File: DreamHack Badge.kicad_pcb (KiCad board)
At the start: 2 copper layers, 185.4 x 124.5 mm, 0 parts

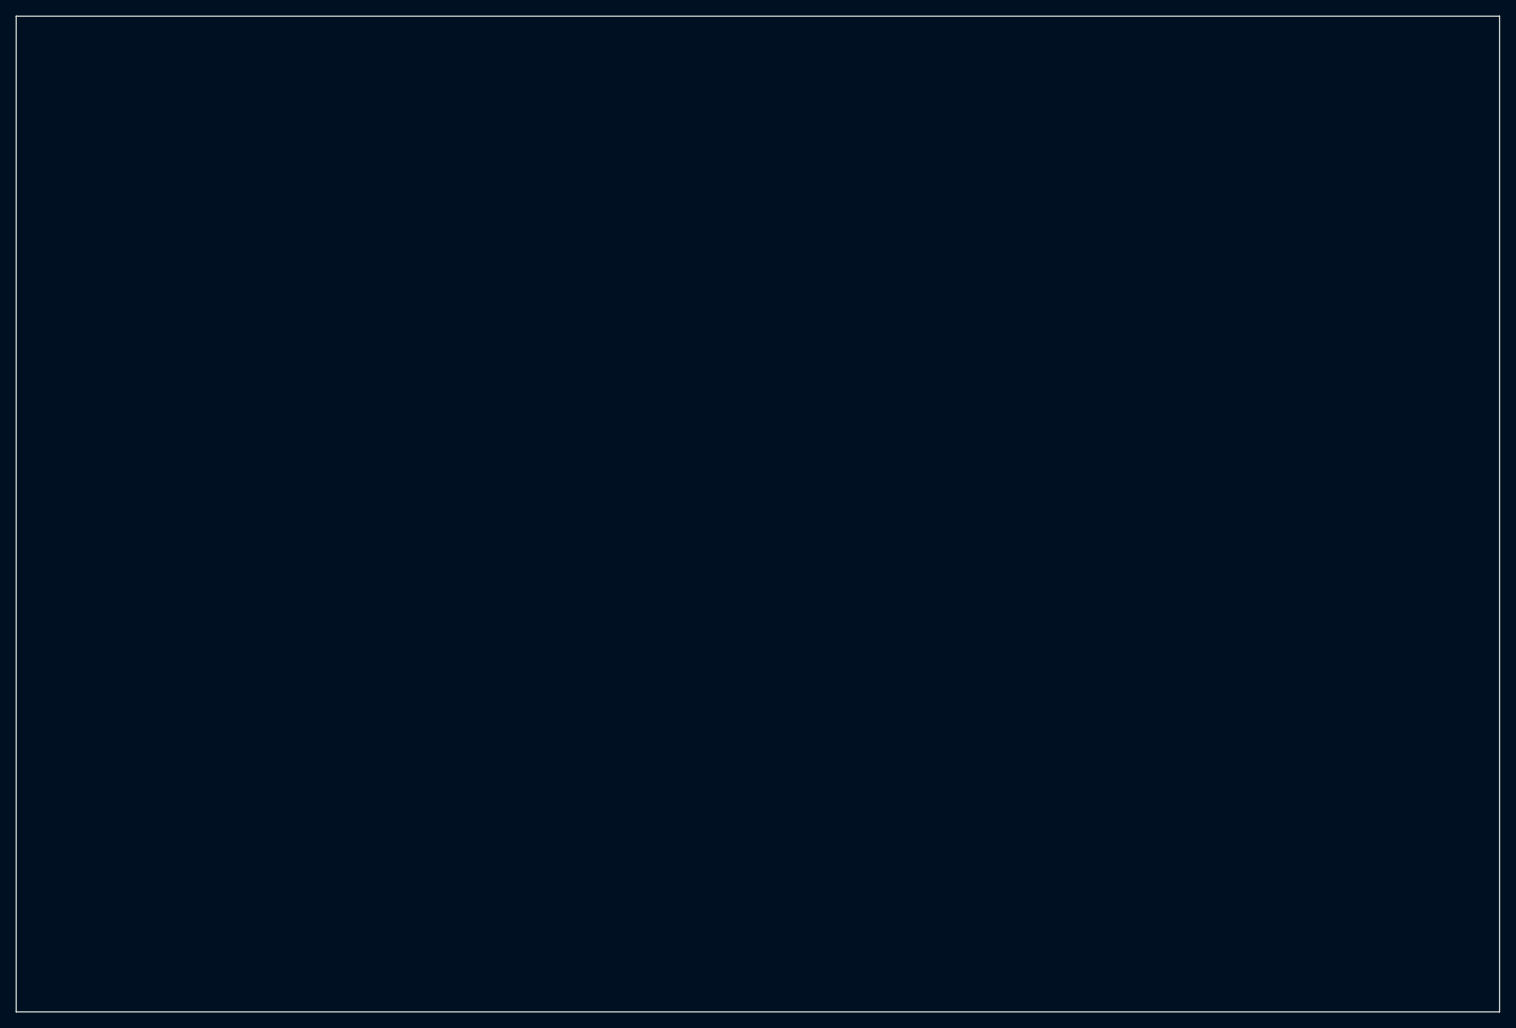
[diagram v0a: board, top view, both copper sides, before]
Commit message: fixed apa102 refs
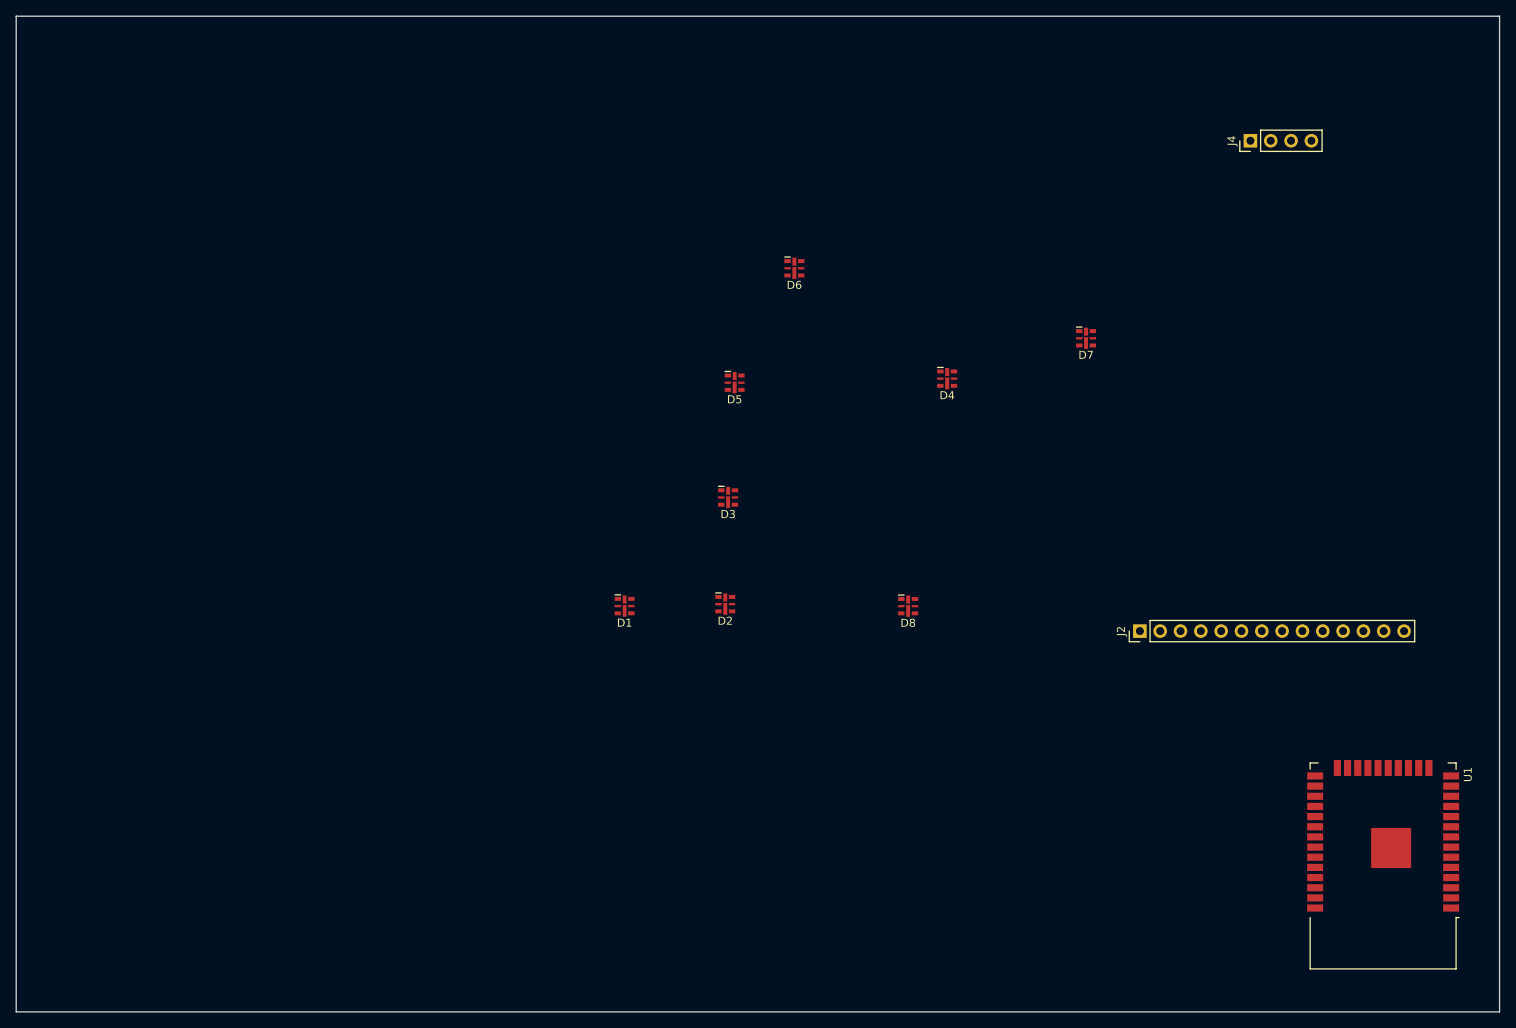
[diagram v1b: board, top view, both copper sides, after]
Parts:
- added D1: APA102-2020, LED_SMD:LED-APA102-2020, F.Cu at (121.8, 99.1)
- added D2: APA102-2020, LED_SMD:LED-APA102-2020, F.Cu at (134.4, 98.9)
- added D3: APA102-2020, LED_SMD:LED-APA102-2020, F.Cu at (134.7, 85.6)
- added D4: APA102-2020, LED_SMD:LED-APA102-2020, F.Cu at (162.1, 70.7)
- added D5: APA102-2020, LED_SMD:LED-APA102-2020, F.Cu at (135.5, 71.2)
- added D6: APA102-2020, LED_SMD:LED-APA102-2020, F.Cu at (143.0, 56.9)
- added D7: APA102-2020, LED_SMD:LED-APA102-2020, F.Cu at (179.5, 65.7)
- added D8: APA102-2020, LED_SMD:LED-APA102-2020, F.Cu at (157.2, 99.2)
- added J2: Conn_01x14_Female, Pin_Headers:Pin_Header_Straight_1x14_Pitch2.54mm, F.Cu at (186.2, 102.3)
- added J4: Conn_01x04_Female, Pin_Headers:Pin_Header_Straight_1x04_Pitch2.54mm, F.Cu at (200.0, 41.0)
- added U1: ESP32-WROOM-32, RF_Modules_Local:ESP32-WROOM-32, F.Cu at (216.6, 128.6)

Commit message: basic pcb layout
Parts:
- moved D4 122.1 mm to (62.1, 140.8)
- moved D5 82.0 mm to (61.5, 35.9)
- moved D1 74.5 mm to (183.4, 140.9)
- moved D3 63.1 mm to (104.5, 141.0)
- moved D8 63.0 mm to (168.1, 37.1)
- moved D7 51.4 mm to (136.9, 36.9)
- moved D2 43.1 mm to (143.8, 140.9)
- moved D6 41.3 mm to (106.9, 36.8)
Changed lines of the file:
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@@
   )
   (module LED_SMD:LED-APA102-2020 (layer F.Cu)
-    (at 157.2124 99.1506)
+    (at 168.148 37.1094)
     (descr http://www.led-color.com/upload/201604/APA102-2020%20SMD%20LED.pdf)
     (tags "LED RGB SPI")
@@
   )
   (module LED_SMD:LED-APA102-2020 (layer F.Cu)
-    (at 162.091 70.7026)
+    (at 62.0776 140.8176)
     (descr http://www.led-color.com/upload/201604/APA102-2020%20SMD%20LED.pdf)
     (tags "LED RGB SPI")
@@
   )
   (module LED_SMD:LED-APA102-2020 (layer F.Cu)
-    (at 179.451 65.659)
+    (at 136.8688 36.946)
     (descr http://www.led-color.com/upload/201604/APA102-2020%20SMD%20LED.pdf)
     (tags "LED RGB SPI")
@@
   )
   (module LED_SMD:LED-APA102-2020 (layer F.Cu)
-    (at 134.7098 85.5616)
+    (at 104.521 141.0208)
     (descr http://www.led-color.com/upload/201604/APA102-2020%20SMD%20LED.pdf)
     (tags "LED RGB SPI")
@@
   )
   (module LED_SMD:LED-APA102-2020 (layer F.Cu)
-    (at 142.9884 56.9104)
+    (at 106.8578 36.8046)
     (descr http://www.led-color.com/upload/201604/APA102-2020%20SMD%20LED.pdf)
     (tags "LED RGB SPI")
@@
   )
   (module LED_SMD:LED-APA102-2020 (layer F.Cu)
-    (at 134.3542 98.8966)
+    (at 143.8402 140.9192)
     (descr http://www.led-color.com/upload/201604/APA102-2020%20SMD%20LED.pdf)
     (tags "LED RGB SPI")
@@
   )
   (module LED_SMD:LED-APA102-2020 (layer F.Cu)
-    (at 135.5208 71.2106)
+    (at 61.5188 35.8902)
     (descr http://www.led-color.com/upload/201604/APA102-2020%20SMD%20LED.pdf)
     (tags "LED RGB SPI")
@@
   )
   (module LED_SMD:LED-APA102-2020 (layer F.Cu)
-    (at 121.7676 99.1362)
-    (descr http://www.led-color.com/upload/201604/APA102-2020%20SMD%20LED.pdf)
-    (tags "LED RGB SPI")
+    (at 183.4388 140.9192)
+    (descr http://www.led-color.com/upload/201604/APA102-2020%20SMD%20LED.pdf)
+    (tags "LED RGB SPI")

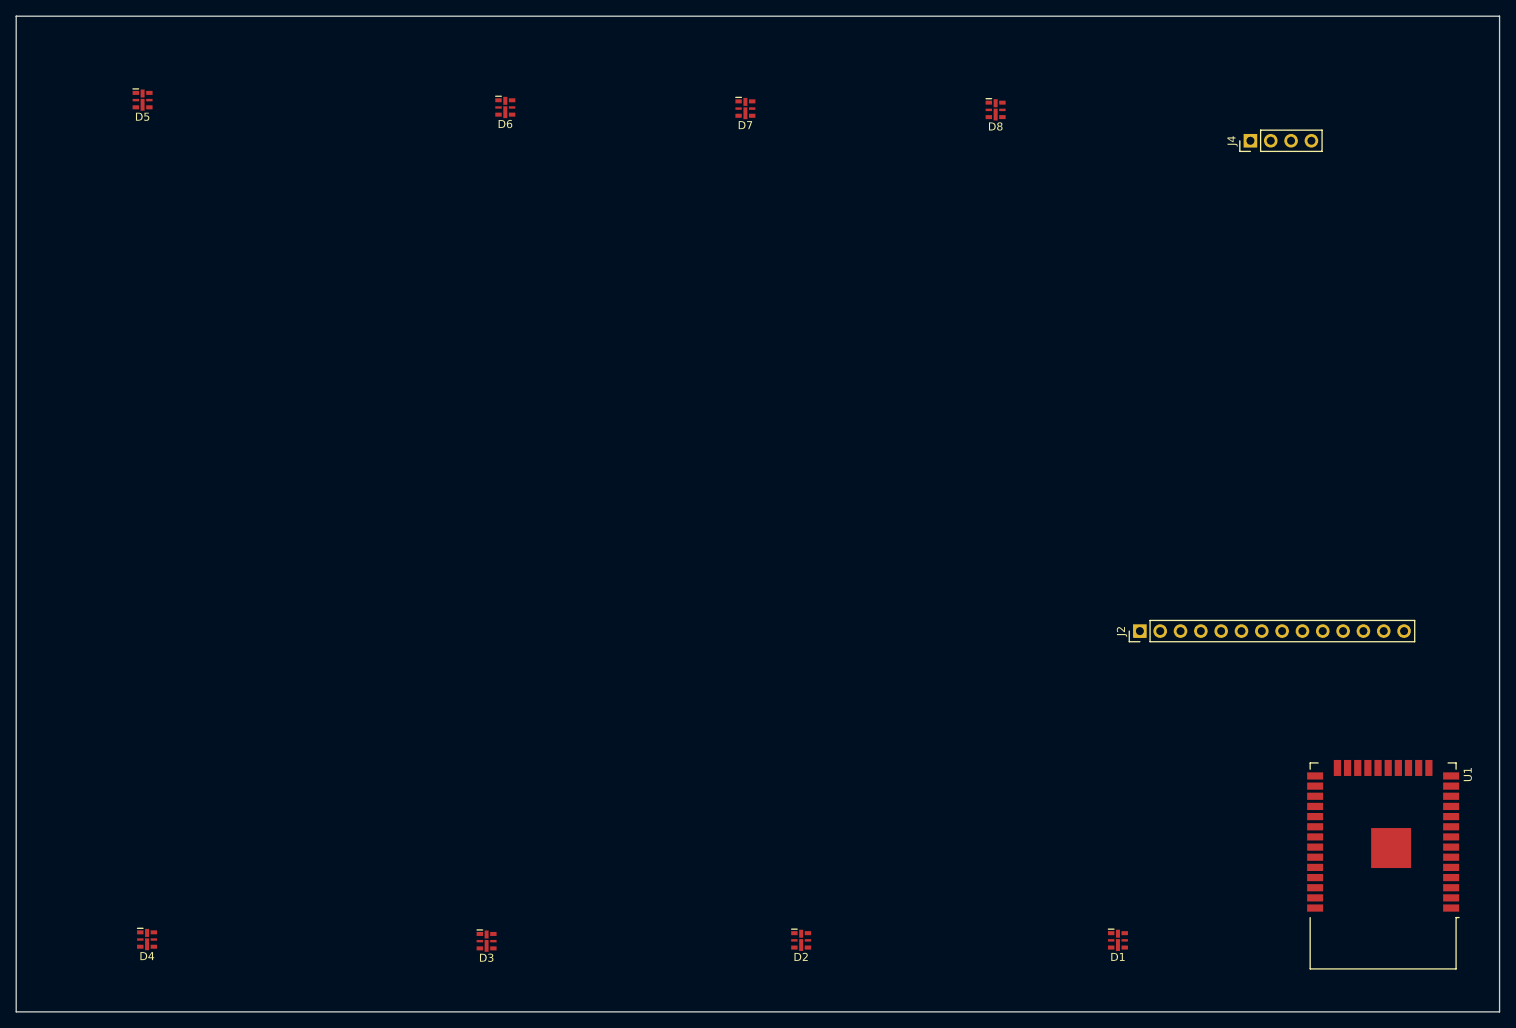
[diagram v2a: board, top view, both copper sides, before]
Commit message: updated pcb, added cutout and moved esp to back
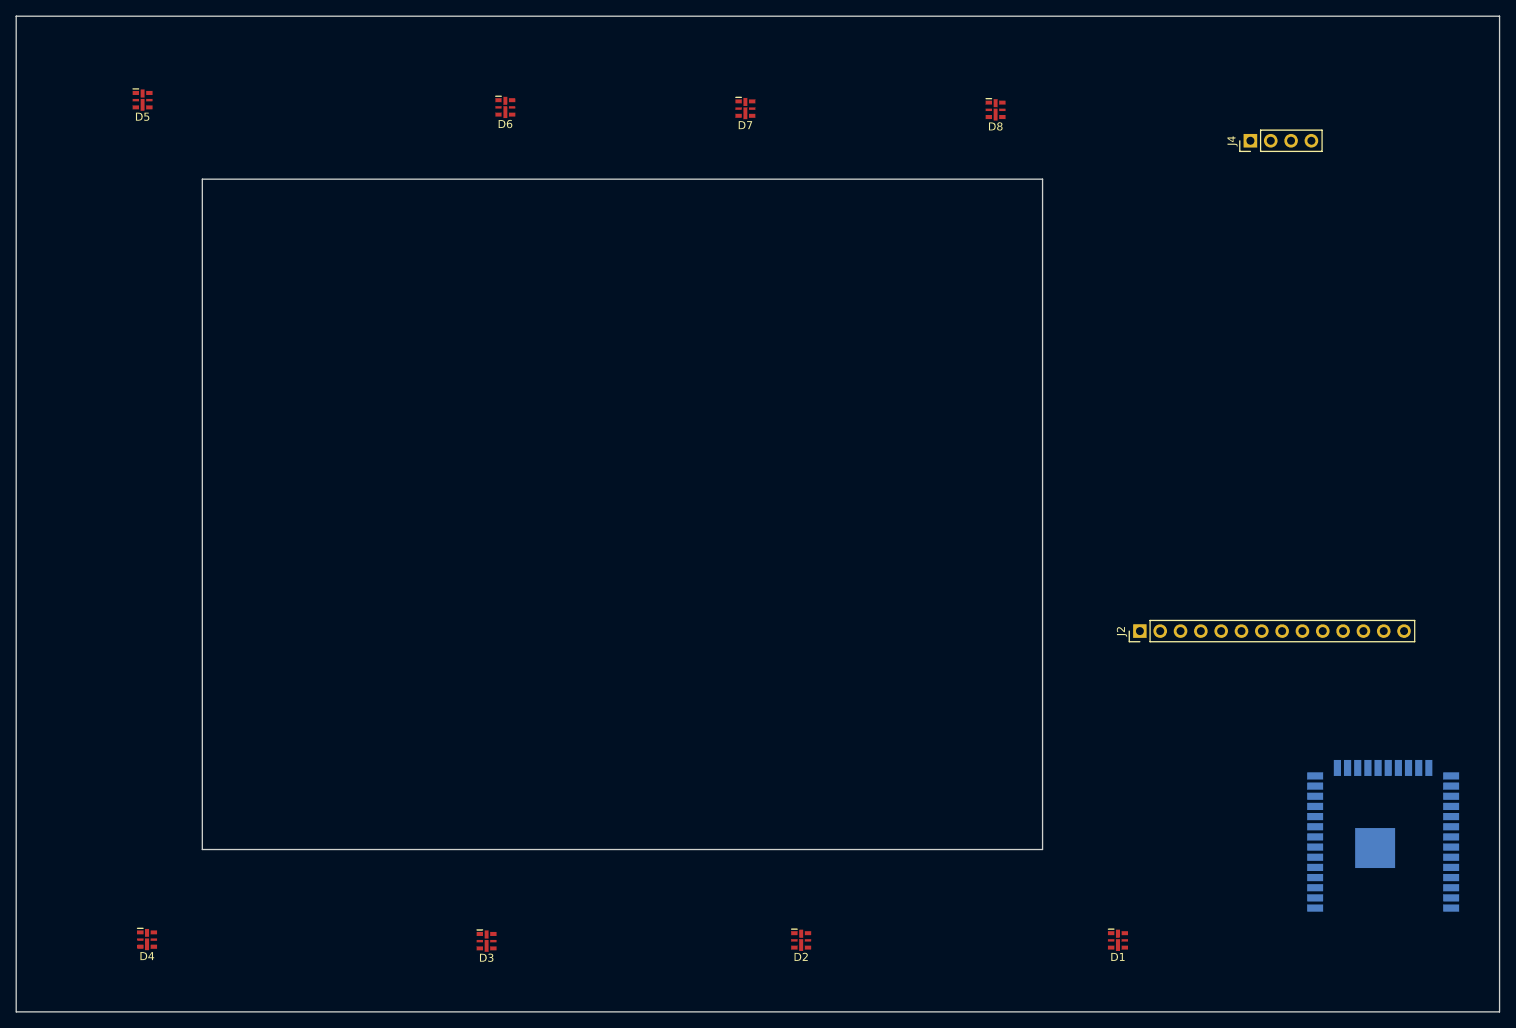
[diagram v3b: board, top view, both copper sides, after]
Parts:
- U1: moved to B.Cu
- turned U1 to 0 degrees
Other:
- outline, holes or cut-outs redrawn

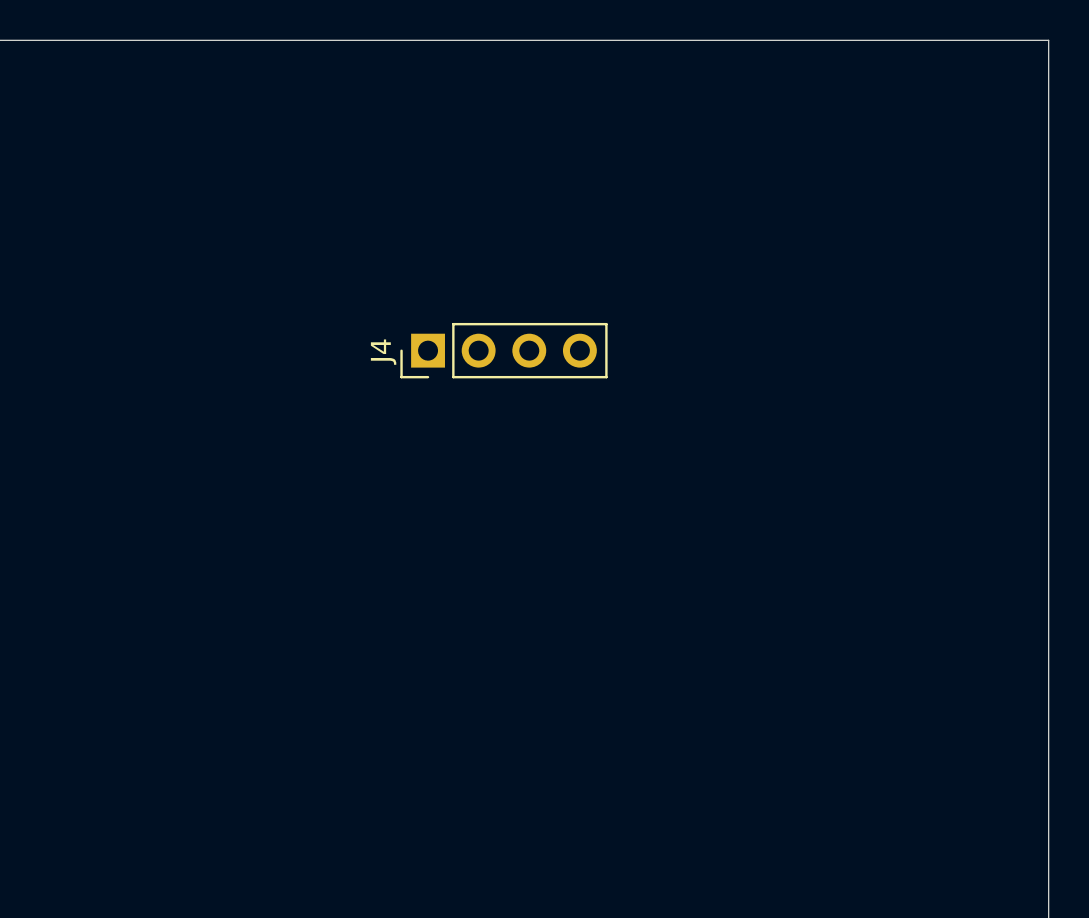
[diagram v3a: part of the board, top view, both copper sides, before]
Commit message: Updated PCB with power and serial components
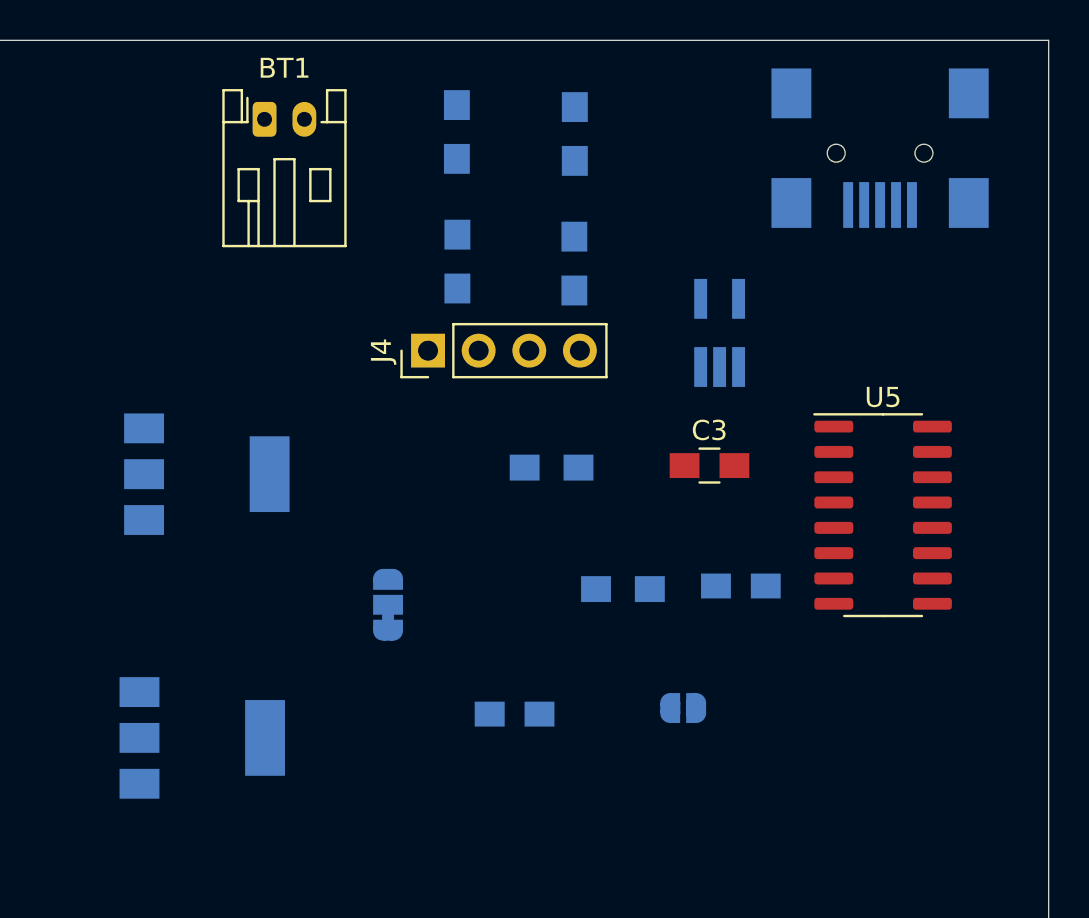
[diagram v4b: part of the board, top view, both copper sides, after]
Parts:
- added BT1: Battery, Connector_JST:JST_PH_S2B-PH-K_1x02_P2.00mm_Horizontal, F.Cu at (191.8, 29.4)
- added C1: 10μF, Capacitors_SMD:C_0805_HandSoldering, B.Cu at (204.3, 59.2)
- added C2: 10μF, Capacitors_SMD:C_0805_HandSoldering, B.Cu at (215.7, 52.8)
- added C3: 10nf, Capacitors_SMD:C_0805_HandSoldering, F.Cu at (214.1, 46.7)
- added D10: Green LED, LEDs:LED_0805_HandSoldering, B.Cu at (207.4, 30.1)
- added D9: Red LED, LEDs:LED_0805_HandSoldering, B.Cu at (201.4, 30.0)
- added J1: USB_B_Mini, Connectors:USB_Mini-B, B.Cu at (222.7, 30.9)
- added JP1: SolderJumper_3_Bridged12, Jumper:SolderJumper-3_P1.3mm_Bridged12_RoundedPad1.0x1.5mm, B.Cu at (198.0, 53.7)
- added JP2: SolderJumper_2_Open, Jumper:SolderJumper-2_P1.3mm_Open_RoundedPad1.0x1.5mm, B.Cu at (212.8, 58.9)
- added R1: 478, Resistors_SMD:R_0805_HandSoldering, B.Cu at (201.5, 36.5)
- added R2: 478, Resistors_SMD:R_0805_HandSoldering, B.Cu at (207.3, 36.6)
- added R3: 2.5K, Resistors_SMD:R_0805_HandSoldering, B.Cu at (206.2, 46.8)
- added R4: 10K, Resistors_SMD:R_0805_HandSoldering, B.Cu at (209.8, 52.9)
- added U2: AMS1117-3.3, TO_SOT_Packages_SMD:SOT-223-3_TabPin2, B.Cu at (188.9, 47.2)
- added U3: AMS1117-5.0, TO_SOT_Packages_SMD:SOT-223-3_TabPin2, B.Cu at (188.7, 60.4)
- added U4: MCP73831-2-OT, TO_SOT_Packages_SMD:TSOT-23-5_HandSoldering, B.Cu at (214.6, 40.1)
- added U5: CH340G, Package_SO:SOIC-16_3.9x9.9mm_P1.27mm, F.Cu at (222.8, 49.2)
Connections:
- D1 pad 1: +3V3 -> +VSW
- D2 pad 1: +3V3 -> +VSW
- D3 pad 1: +3V3 -> +VSW
- D4 pad 1: +3V3 -> +VSW
- D5 pad 1: +3V3 -> +VSW
- D6 pad 1: +3V3 -> +VSW
- D7 pad 1: +3V3 -> +VSW
- D8 pad 1: +3V3 -> +VSW
- J2 pad 1: +3V3 -> /VCC
- U1 pad 34: Net-(U1-Pad34) -> /Serial_TXD
- U1 pad 35: Net-(U1-Pad35) -> /Serial_RXD
